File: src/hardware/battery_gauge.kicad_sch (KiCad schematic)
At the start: 0 parts

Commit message: Added Gauge
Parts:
- added C20: 1µF, symbol Device:C
- added C21: 470nF, symbol Device:C
- added C22: 2.2µF, symbol Device:C
- added R7: 10m, symbol Device:R
- added R8, R9: 10k, symbol Device:R
- added U1: BQ27426YZFR, YZF0009AKAL, symbol BQ27426YZFR:BQ27426YZFR
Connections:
- new net: R8.2, U1.A1 (GPOUT)
- new net: R9.2, U1.B1 (BIN)
- new net +1V8: C21.2, C22.2, R8.1, U1.B3 (VDD)
- new net +BATT: C20.2, R7.1, U1.C1 (SRP), U1.C3 (BAT)
- new net GND: C20.1, C21.1, C22.1, R9.1, U1.B2 (VSS)
- new net SCL1V8: U1.A3 (SCL)
- new net SDA1V8: U1.A2 (SDA)
- new net VBAT: R7.2, U1.C2 (SRN)
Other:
- note added: "I²C: 1010101"

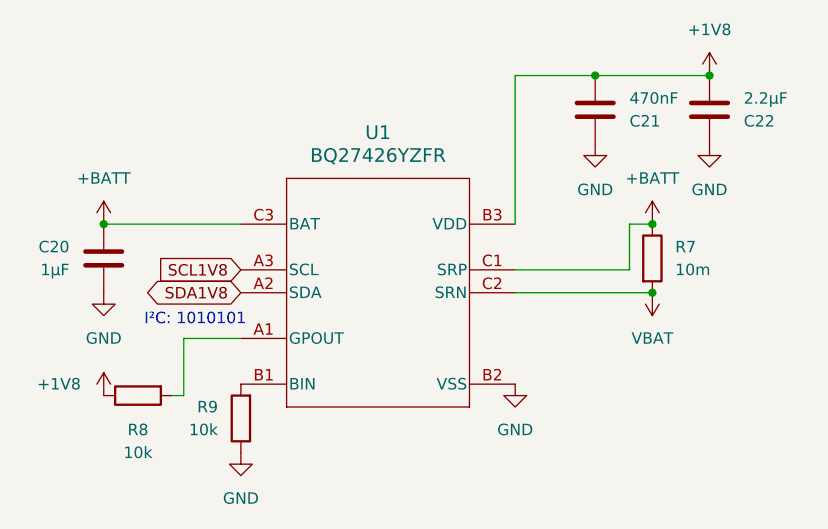
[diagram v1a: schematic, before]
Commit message: Added Accelerometer Clock; Cleanup & Fixes
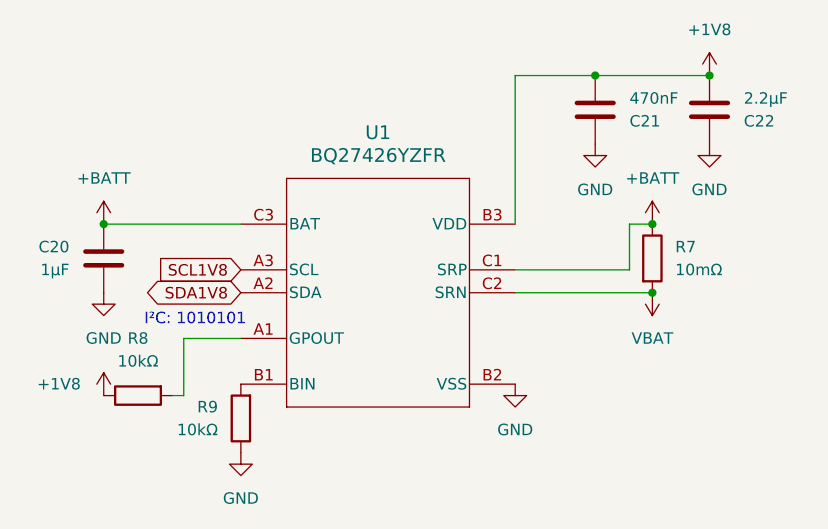
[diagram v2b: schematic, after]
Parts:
- R7: value 10m -> 10mΩ; Sense 1% -> (none); Tolerance (none) -> 1%
- R8, R9: value 10k -> 10kΩ
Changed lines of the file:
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@@
 		(fields_autoplaced yes)
 		(property "Reference" "R8"
-			(at 113.03 116.84 90)
-			(effects
-				(font
-					(size 1.27 1.27)
-				)
-			)
-		)
-		(property "Value" "10k"
-			(at 113.03 119.38 90)
+			(at 113.03 106.68 90)
+			(effects
+				(font
+					(size 1.27 1.27)
+				)
+			)
+		)
+		(property "Value" "10kΩ"
+			(at 113.03 109.22 90)
 			(effects
 				(font
@@
 			)
 		)
-		(property "Value" "10m"
+		(property "Value" "10mΩ"
 			(at 172.72 99.0599 0)
 			(effects
@@
 			)
 		)
-		(property "Sense" "1%"
+		(property "Tolerance" "1%"
 			(at 170.18 97.79 0)
 			(effects
@@
 			)
 		)
-		(property "Value" "10k"
+		(property "Value" "10kΩ"
 			(at 121.92 116.8399 0)
 			(effects

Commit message: Cleanup & Fixes; Added footprints; Removed Light sensors
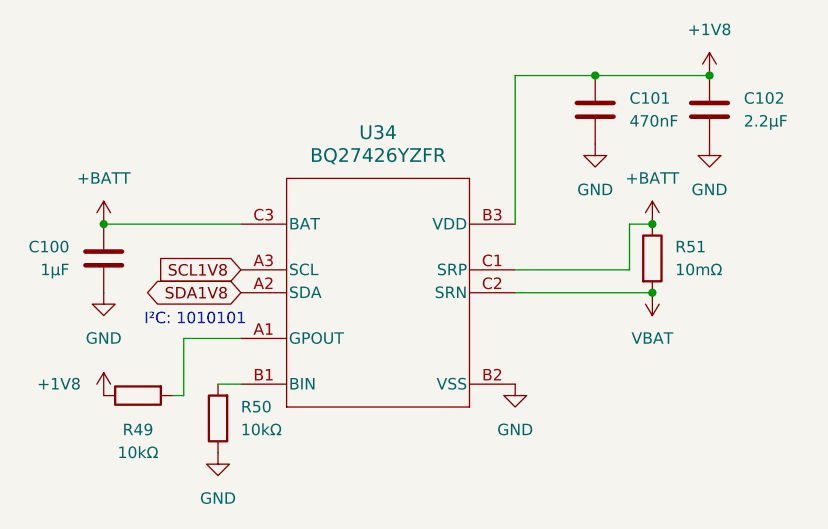
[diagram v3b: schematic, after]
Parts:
- C100: renamed from C20; footprint (none) -> Capacitor_SMD:C_0603_1608Metric
- C101: renamed from C21; footprint (none) -> Capacitor_SMD:C_0603_1608Metric
- C102: renamed from C22; footprint (none) -> Capacitor_SMD:C_0603_1608Metric
- R49: renamed from R8; footprint (none) -> Resistor_SMD:R_0603_1608Metric
- R50: renamed from R9; footprint (none) -> Resistor_SMD:R_0603_1608Metric
- R51: renamed from R7; footprint (none) -> Resistor_SMD:R_0603_1608Metric
- U34: renamed from U1; footprint YZF0009AKAL -> Project:IC_BQ27421YZFR-G1A
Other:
- moved on the sheet: R50

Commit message: Cleanup & Fixes; Changed GPIO; Added Camera; Added Microphone
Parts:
- renumbered C102 to C100, C100 to C98, C101 to C99, R49 to R47, R50 to R48, R51 to R49
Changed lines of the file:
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@@
 		(dnp no)
 		(fields_autoplaced yes)
-		(property "Reference" "#PWR0408"
+		(property "Reference" "#PWR0404"
 			(at 170.18 97.79 0)
 			(effects
@@
 			(project "raywatch"
 				(path "/7b654ee8-2a53-4d39-8b7d-32c7bb3cb0ed/6e6a70ea-4db2-4b59-a2d7-c468f9b8b5a6/27d482b0-7b63-432c-88d1-098048a1418a"
-					(reference "#PWR0408")
+					(reference "#PWR0404")
 					(unit 1)
 				)
@@
 		(dnp no)
 		(fields_autoplaced yes)
-		(property "Reference" "R49"
+		(property "Reference" "R47"
 			(at 113.03 116.84 90)
 			(effects
@@
 			(project "raywatch"
 				(path "/7b654ee8-2a53-4d39-8b7d-32c7bb3cb0ed/6e6a70ea-4db2-4b59-a2d7-c468f9b8b5a6/27d482b0-7b63-432c-88d1-098048a1418a"
-					(reference "R49")
+					(reference "R47")
 					(unit 1)
 				)
@@
 		(dnp no)
 		(fields_autoplaced yes)
-		(property "Reference" "#PWR0406"
+		(property "Reference" "#PWR0402"
 			(at 154.94 118.11 0)
 			(effects
@@
 			(project "raywatch"
 				(path "/7b654ee8-2a53-4d39-8b7d-32c7bb3cb0ed/6e6a70ea-4db2-4b59-a2d7-c468f9b8b5a6/27d482b0-7b63-432c-88d1-098048a1418a"
-					(reference "#PWR0406")
+					(reference "#PWR0402")
 					(unit 1)
 				)
@@
 		(dnp no)
 		(fields_autoplaced yes)
-		(property "Reference" "#PWR0401"
+		(property "Reference" "#PWR0397"
 			(at 109.22 107.95 0)
 			(effects
@@
 			(project "raywatch"
 				(path "/7b654ee8-2a53-4d39-8b7d-32c7bb3cb0ed/6e6a70ea-4db2-4b59-a2d7-c468f9b8b5a6/27d482b0-7b63-432c-88d1-098048a1418a"
-					(reference "#PWR0401")
+					(reference "#PWR0397")
 					(unit 1)
 				)
@@
 		(dnp no)
 		(fields_autoplaced yes)
-		(property "Reference" "C101"
+		(property "Reference" "C99"
 			(at 167.64 80.0099 0)
 			(effects
@@
 			(project "raywatch"
 				(path "/7b654ee8-2a53-4d39-8b7d-32c7bb3cb0ed/6e6a70ea-4db2-4b59-a2d7-c468f9b8b5a6/27d482b0-7b63-432c-88d1-098048a1418a"
-					(reference "C101")
+					(reference "C99")
 					(unit 1)
 				)
@@
 		(dnp no)
 		(fields_autoplaced yes)
-		(property "Reference" "C100"
+		(property "Reference" "C98"
 			(at 105.41 96.5199 0)
 			(effects
@@
 			(project "raywatch"
 				(path "/7b654ee8-2a53-4d39-8b7d-32c7bb3cb0ed/6e6a70ea-4db2-4b59-a2d7-c468f9b8b5a6/27d482b0-7b63-432c-88d1-098048a1418a"
-					(reference "C100")
+					(reference "C98")
 					(unit 1)
 				)
@@
 		(dnp no)
 		(fields_autoplaced yes)
-		(property "Reference" "#PWR0403"
+		(property "Reference" "#PWR0399"
 			(at 121.92 125.73 0)
 			(effects
@@
 			(project "raywatch"
 				(path "/7b654ee8-2a53-4d39-8b7d-32c7bb3cb0ed/6e6a70ea-4db2-4b59-a2d7-c468f9b8b5a6/27d482b0-7b63-432c-88d1-098048a1418a"
-					(reference "#PWR0403")
+					(reference "#PWR0399")
 					(unit 1)
 				)
@@
 		(dnp no)
 		(fields_autoplaced yes)
-		(property "Reference" "#PWR0402"
+		(property "Reference" "#PWR0398"
 			(at 109.22 116.84 0)
 			(effects
@@
 			(project "raywatch"
 				(path "/7b654ee8-2a53-4d39-8b7d-32c7bb3cb0ed/6e6a70ea-4db2-4b59-a2d7-c468f9b8b5a6/27d482b0-7b63-432c-88d1-098048a1418a"
-					(reference "#PWR0402")
+					(reference "#PWR0398")
 					(unit 1)
 				)
@@
 		(dnp no)
 		(fields_autoplaced yes)
-		(property "Reference" "#PWR0410"
+		(property "Reference" "#PWR0406"
 			(at 176.53 81.28 0)
 			(effects
@@
 			(project "raywatch"
 				(path "/7b654ee8-2a53-4d39-8b7d-32c7bb3cb0ed/6e6a70ea-4db2-4b59-a2d7-c468f9b8b5a6/27d482b0-7b63-432c-88d1-098048a1418a"
-					(reference "#PWR0410")
+					(reference "#PWR0406")
 					(unit 1)
 				)
@@
 		(dnp no)
 		(fields_autoplaced yes)
-		(property "Reference" "#PWR0409"
+		(property "Reference" "#PWR0405"
 			(at 170.18 97.79 0)
 			(effects
@@
 			(project "raywatch"
 				(path "/7b654ee8-2a53-4d39-8b7d-32c7bb3cb0ed/6e6a70ea-4db2-4b59-a2d7-c468f9b8b5a6/27d482b0-7b63-432c-88d1-098048a1418a"
-					(reference "#PWR0409")
+					(reference "#PWR0405")
 					(unit 1)
 				)
@@
 		(dnp no)
 		(fields_autoplaced yes)
-		(property "Reference" "#PWR0411"
+		(property "Reference" "#PWR0407"
 			(at 176.53 91.44 0)
 			(effects
@@
 			(project "raywatch"
 				(path "/7b654ee8-2a53-4d39-8b7d-32c7bb3cb0ed/6e6a70ea-4db2-4b59-a2d7-c468f9b8b5a6/27d482b0-7b63-432c-88d1-098048a1418a"
-					(reference "#PWR0411")
+					(reference "#PWR0407")
 					(unit 1)
 				)
@@
 		(dnp no)
 		(fields_autoplaced yes)
-		(property "Reference" "#PWR0407"
+		(property "Reference" "#PWR0403"
 			(at 163.83 91.44 0)
 			(effects
@@
 			(project "raywatch"
 				(path "/7b654ee8-2a53-4d39-8b7d-32c7bb3cb0ed/6e6a70ea-4db2-4b59-a2d7-c468f9b8b5a6/27d482b0-7b63-432c-88d1-098048a1418a"
-					(reference "#PWR0407")
+					(reference "#PWR0403")
 					(unit 1)
 				)
@@
 		(dnp no)
 		(fields_autoplaced yes)
-		(property "Reference" "R51"
+		(property "Reference" "R49"
 			(at 172.72 96.5199 0)
 			(effects
@@
 			(project "raywatch"
 				(path "/7b654ee8-2a53-4d39-8b7d-32c7bb3cb0ed/6e6a70ea-4db2-4b59-a2d7-c468f9b8b5a6/27d482b0-7b63-432c-88d1-098048a1418a"
-					(reference "R51")
+					(reference "R49")
 					(unit 1)
 				)
@@
 		(dnp no)
 		(fields_autoplaced yes)
-		(property "Reference" "R50"
+		(property "Reference" "R48"
 			(at 124.46 114.2999 0)
 			(effects
@@
 			(project "raywatch"
 				(path "/7b654ee8-2a53-4d39-8b7d-32c7bb3cb0ed/6e6a70ea-4db2-4b59-a2d7-c468f9b8b5a6/27d482b0-7b63-432c-88d1-098048a1418a"
-					(reference "R50")
+					(reference "R48")
 					(unit 1)
 				)
@@
 		(dnp no)
 		(fields_autoplaced yes)
-		(property "Reference" "C102"
+		(property "Reference" "C100"
 			(at 180.34 80.0099 0)
 			(effects
@@
 			(project "raywatch"
 				(path "/7b654ee8-2a53-4d39-8b7d-32c7bb3cb0ed/6e6a70ea-4db2-4b59-a2d7-c468f9b8b5a6/27d482b0-7b63-432c-88d1-098048a1418a"
-					(reference "C102")
+					(reference "C100")
 					(unit 1)
 				)
@@
 		(dnp no)
 		(fields_autoplaced yes)
-		(property "Reference" "#PWR0400"
+		(property "Reference" "#PWR0396"
 			(at 109.22 97.79 0)
 			(effects
@@
 			(project "raywatch"
 				(path "/7b654ee8-2a53-4d39-8b7d-32c7bb3cb0ed/6e6a70ea-4db2-4b59-a2d7-c468f9b8b5a6/27d482b0-7b63-432c-88d1-098048a1418a"
-					(reference "#PWR0400")
-					(unit 1)
-				)
+					(reference "#PWR0396")
+					(unit 1)
+				)

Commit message: Add Light Sensor and Proximity & Gesture Sensor; Changed GPIO
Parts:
- renumbered R47 to R48, R48 to R49, R49 to R50
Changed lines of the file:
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@@
 		(dnp no)
 		(fields_autoplaced yes)
-		(property "Reference" "#PWR0404"
+		(property "Reference" "#PWR0406"
 			(at 170.18 97.79 0)
 			(effects
@@
 			(project "raywatch"
 				(path "/7b654ee8-2a53-4d39-8b7d-32c7bb3cb0ed/6e6a70ea-4db2-4b59-a2d7-c468f9b8b5a6/27d482b0-7b63-432c-88d1-098048a1418a"
-					(reference "#PWR0404")
+					(reference "#PWR0406")
 					(unit 1)
 				)
@@
 		(dnp no)
 		(fields_autoplaced yes)
-		(property "Reference" "R47"
+		(property "Reference" "R48"
 			(at 113.03 116.84 90)
 			(effects
@@
 			(project "raywatch"
 				(path "/7b654ee8-2a53-4d39-8b7d-32c7bb3cb0ed/6e6a70ea-4db2-4b59-a2d7-c468f9b8b5a6/27d482b0-7b63-432c-88d1-098048a1418a"
-					(reference "R47")
+					(reference "R48")
 					(unit 1)
 				)
@@
 		(dnp no)
 		(fields_autoplaced yes)
-		(property "Reference" "#PWR0402"
+		(property "Reference" "#PWR0404"
 			(at 154.94 118.11 0)
 			(effects
@@
 			(project "raywatch"
 				(path "/7b654ee8-2a53-4d39-8b7d-32c7bb3cb0ed/6e6a70ea-4db2-4b59-a2d7-c468f9b8b5a6/27d482b0-7b63-432c-88d1-098048a1418a"
-					(reference "#PWR0402")
+					(reference "#PWR0404")
 					(unit 1)
 				)
@@
 		(dnp no)
 		(fields_autoplaced yes)
-		(property "Reference" "#PWR0397"
+		(property "Reference" "#PWR0399"
 			(at 109.22 107.95 0)
 			(effects
@@
 			(project "raywatch"
 				(path "/7b654ee8-2a53-4d39-8b7d-32c7bb3cb0ed/6e6a70ea-4db2-4b59-a2d7-c468f9b8b5a6/27d482b0-7b63-432c-88d1-098048a1418a"
-					(reference "#PWR0397")
+					(reference "#PWR0399")
 					(unit 1)
 				)
@@
 		(dnp no)
 		(fields_autoplaced yes)
-		(property "Reference" "#PWR0399"
+		(property "Reference" "#PWR0401"
 			(at 121.92 125.73 0)
 			(effects
@@
 			(project "raywatch"
 				(path "/7b654ee8-2a53-4d39-8b7d-32c7bb3cb0ed/6e6a70ea-4db2-4b59-a2d7-c468f9b8b5a6/27d482b0-7b63-432c-88d1-098048a1418a"
-					(reference "#PWR0399")
+					(reference "#PWR0401")
 					(unit 1)
 				)
@@
 		(dnp no)
 		(fields_autoplaced yes)
-		(property "Reference" "#PWR0398"
+		(property "Reference" "#PWR0400"
 			(at 109.22 116.84 0)
 			(effects
@@
 			(project "raywatch"
 				(path "/7b654ee8-2a53-4d39-8b7d-32c7bb3cb0ed/6e6a70ea-4db2-4b59-a2d7-c468f9b8b5a6/27d482b0-7b63-432c-88d1-098048a1418a"
-					(reference "#PWR0398")
+					(reference "#PWR0400")
 					(unit 1)
 				)
@@
 		(dnp no)
 		(fields_autoplaced yes)
-		(property "Reference" "#PWR0406"
+		(property "Reference" "#PWR0408"
 			(at 176.53 81.28 0)
 			(effects
@@
 			(project "raywatch"
 				(path "/7b654ee8-2a53-4d39-8b7d-32c7bb3cb0ed/6e6a70ea-4db2-4b59-a2d7-c468f9b8b5a6/27d482b0-7b63-432c-88d1-098048a1418a"
-					(reference "#PWR0406")
+					(reference "#PWR0408")
 					(unit 1)
 				)
@@
 		(dnp no)
 		(fields_autoplaced yes)
-		(property "Reference" "#PWR0405"
+		(property "Reference" "#PWR0407"
 			(at 170.18 97.79 0)
 			(effects
@@
 			(project "raywatch"
 				(path "/7b654ee8-2a53-4d39-8b7d-32c7bb3cb0ed/6e6a70ea-4db2-4b59-a2d7-c468f9b8b5a6/27d482b0-7b63-432c-88d1-098048a1418a"
-					(reference "#PWR0405")
+					(reference "#PWR0407")
 					(unit 1)
 				)
@@
 		(dnp no)
 		(fields_autoplaced yes)
-		(property "Reference" "#PWR0407"
+		(property "Reference" "#PWR0409"
 			(at 176.53 91.44 0)
 			(effects
@@
 			(project "raywatch"
 				(path "/7b654ee8-2a53-4d39-8b7d-32c7bb3cb0ed/6e6a70ea-4db2-4b59-a2d7-c468f9b8b5a6/27d482b0-7b63-432c-88d1-098048a1418a"
-					(reference "#PWR0407")
+					(reference "#PWR0409")
 					(unit 1)
 				)
@@
 		(dnp no)
 		(fields_autoplaced yes)
-		(property "Reference" "#PWR0403"
+		(property "Reference" "#PWR0405"
 			(at 163.83 91.44 0)
 			(effects
@@
 			(project "raywatch"
 				(path "/7b654ee8-2a53-4d39-8b7d-32c7bb3cb0ed/6e6a70ea-4db2-4b59-a2d7-c468f9b8b5a6/27d482b0-7b63-432c-88d1-098048a1418a"
-					(reference "#PWR0403")
+					(reference "#PWR0405")
 					(unit 1)
 				)
@@
 		(dnp no)
 		(fields_autoplaced yes)
-		(property "Reference" "R49"
+		(property "Reference" "R50"
 			(at 172.72 96.5199 0)
 			(effects
@@
 			(project "raywatch"
 				(path "/7b654ee8-2a53-4d39-8b7d-32c7bb3cb0ed/6e6a70ea-4db2-4b59-a2d7-c468f9b8b5a6/27d482b0-7b63-432c-88d1-098048a1418a"
-					(reference "R49")
+					(reference "R50")
 					(unit 1)
 				)
@@
 		(dnp no)
 		(fields_autoplaced yes)
-		(property "Reference" "R48"
+		(property "Reference" "R49"
 			(at 124.46 114.2999 0)
 			(effects
@@
 			(project "raywatch"
 				(path "/7b654ee8-2a53-4d39-8b7d-32c7bb3cb0ed/6e6a70ea-4db2-4b59-a2d7-c468f9b8b5a6/27d482b0-7b63-432c-88d1-098048a1418a"
-					(reference "R48")
+					(reference "R49")
 					(unit 1)
 				)
@@
 		(dnp no)
 		(fields_autoplaced yes)
-		(property "Reference" "#PWR0396"
+		(property "Reference" "#PWR0398"
 			(at 109.22 97.79 0)
 			(effects
@@
 			(project "raywatch"
 				(path "/7b654ee8-2a53-4d39-8b7d-32c7bb3cb0ed/6e6a70ea-4db2-4b59-a2d7-c468f9b8b5a6/27d482b0-7b63-432c-88d1-098048a1418a"
-					(reference "#PWR0396")
-					(unit 1)
-				)
+					(reference "#PWR0398")
+					(unit 1)
+				)
